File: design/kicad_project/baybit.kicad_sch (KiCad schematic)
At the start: 89 parts, among them J1 EXT_PWR DNI, J2 USB_B_Micro, J3 ER-TFT1.44-1, J4 EXT_LED DNI, J5 U_FL DNI, J6 MIKROBUS_HOST_CONN 8+8P, Q1 BSD235C, Q2 BC847BS, Q3 BC848, SW1 B3U-1000P, SW2 ALPS_SKRH, SW3 RS282G05A3, SW4 RS282G05A3, U1 TPD2EUSB30A, U2 CP2102N-Axx-GQFN28, U3 XC6220B331MR, U4 WS2811, U5 LSM303AGR, U6 ESP32-PICO-D4, U7 PCF8574-SO16, U8 TSC2007IPW

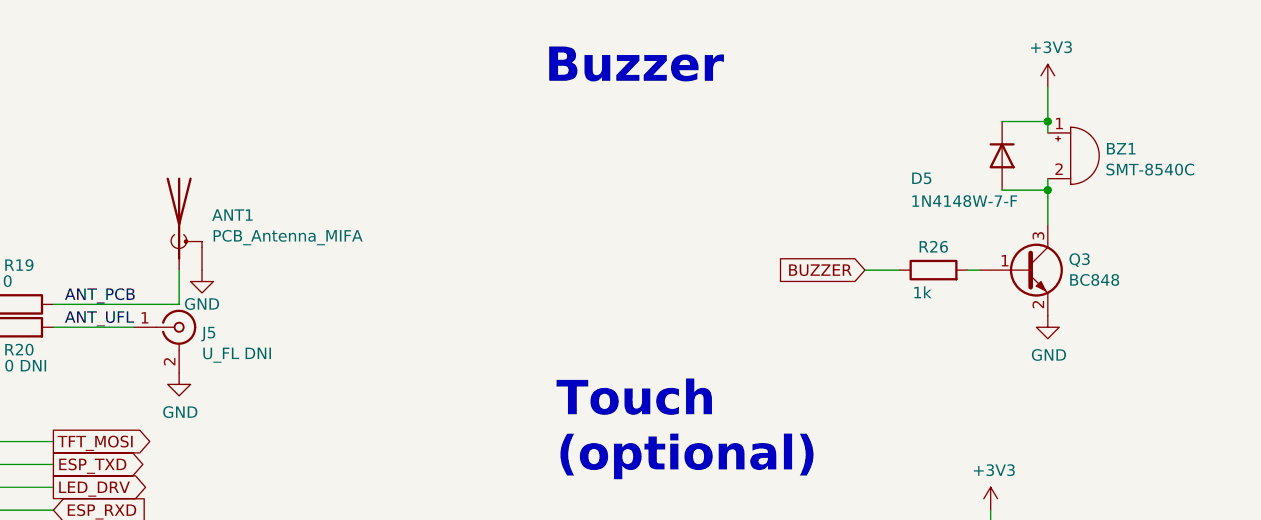
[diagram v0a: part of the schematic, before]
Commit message: Migrated to Kicad 9
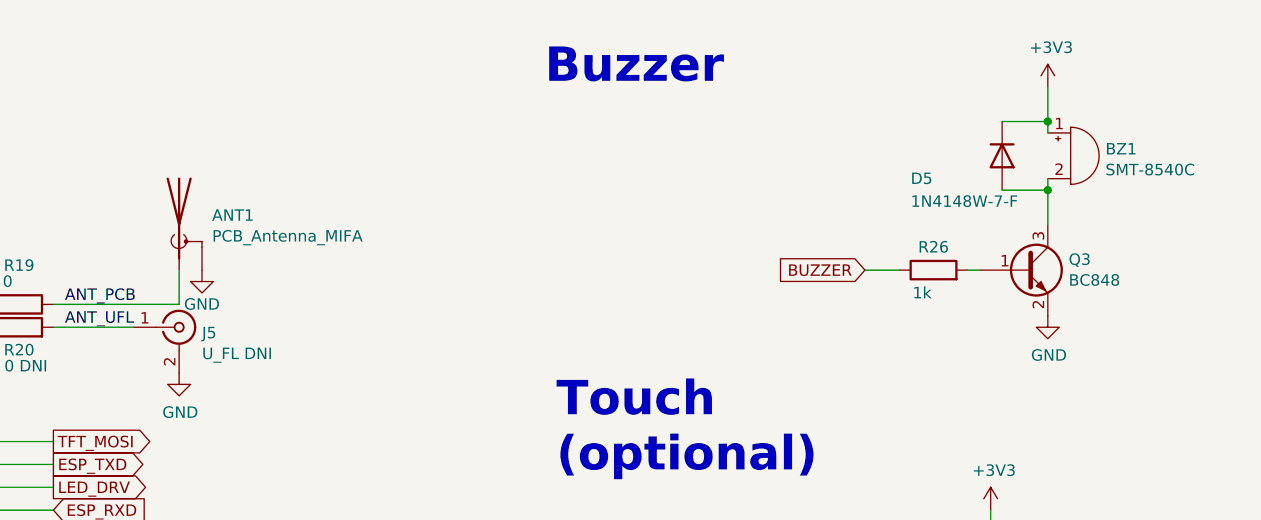
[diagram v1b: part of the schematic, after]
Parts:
- U6: footprint Package_DFN_QFN:QFN-48-1EP_7x7mm_P0.5mm_EP5.3x5.3mm -> Package_DFN_QFN:QFN-48-1EP_7x7mm_P0.5mm_EP5.15x5.15mm
